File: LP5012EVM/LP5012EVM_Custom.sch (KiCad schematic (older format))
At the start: 10 parts, among them J1 Main Connector, U1 LP5012

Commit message: Corrección de errores y actualizacion de nombres
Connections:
- net VBG is gone; now on net VCC: D1.4 (BA), D1.5 (GA), D2.4 (BA), D2.5 (GA), D3.4 (BA), D3.5 (GA), D4.4 (BA), D4.5 (GA)
- net VR is gone; now on net VCC: D1.6 (RA), D2.6 (RA), D3.6 (RA), D4.6 (RA)
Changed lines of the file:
@@
 EESchema Schematic File Version 4
-LIBS:LP5012EVM-cache
 EELAYER 30 0
 EELAYER END
@@
 Text Label 9050 5300 2    50   ~ 0
 LB10
-Text Label 9750 2100 0    50   ~ 0
-VR
-Text Label 9750 2300 0    50   ~ 0
-VBG
-Text Label 9750 2500 0    50   ~ 0
-VBG
-Wire Wire Line
-	9600 2100 9750 2100
-Wire Wire Line
-	9600 2300 9750 2300
-Wire Wire Line
-	9600 2500 9750 2500
-Text Label 9750 4150 0    50   ~ 0
-VR
-Text Label 9750 4350 0    50   ~ 0
-VBG
-Text Label 9750 4550 0    50   ~ 0
-VBG
-Wire Wire Line
-	9600 4150 9750 4150
-Wire Wire Line
-	9600 4350 9750 4350
-Wire Wire Line
-	9600 4550 9750 4550
-Text Label 9750 5100 0    50   ~ 0
-VR
-Text Label 9750 5300 0    50   ~ 0
-VBG
-Text Label 9750 5500 0    50   ~ 0
-VBG
-Wire Wire Line
-	9600 5100 9750 5100
-Wire Wire Line
-	9600 5300 9750 5300
-Wire Wire Line
-	9600 5500 9750 5500
-Text Label 9750 3050 0    50   ~ 0
-VR
-Text Label 9750 3250 0    50   ~ 0
-VBG
-Text Label 9750 3450 0    50   ~ 0
-VBG
-Wire Wire Line
-	9600 3050 9750 3050
-Wire Wire Line
-	9600 3250 9750 3250
-Wire Wire Line
-	9600 3450 9750 3450
 Text Label 7600 7500 0    79   ~ 0
 LP5012_Custom_PCB
@@
 Wire Wire Line
 	5450 3650 5450 3900
-Text Notes 6400 3600 0    50   ~ 0
+Text Notes 5650 4050 0    50   ~ 0
 Via Layout Design from the chip manufacturer.\nPage 45: http://www.ti.com/lit/ds/symlink/lp5012.pdf\n
 Wire Wire Line
@@
 Text Notes 4150 3650 0    50   ~ 0
 Iset(3.3k) = 22.3mA
+$Comp
+L power:VCC #PWR0107
+U 1 1 5D98000B
+P 9900 1950
+F 0 "#PWR0107" H 9900 1800 50  0001 C CNN
+F 1 "VCC" H 9917 2123 50  0000 C CNN
+F 2 "" H 9900 1950 50  0001 C CNN
+F 3 "" H 9900 1950 50  0001 C CNN
+	1    9900 1950
+	1    0    0    -1
+$EndComp
+$Comp
+L power:VCC #PWR0110
+U 1 1 5D981315
+P 9900 2900
+F 0 "#PWR0110" H 9900 2750 50  0001 C CNN
+F 1 "VCC" H 9917 3073 50  0000 C CNN
+F 2 "" H 9900 2900 50  0001 C CNN
+F 3 "" H 9900 2900 50  0001 C CNN
+	1    9900 2900
+	1    0    0    -1
+$EndComp
+$Comp
+L power:VCC #PWR0111
+U 1 1 5D981A4D
+P 9900 4000
+F 0 "#PWR0111" H 9900 3850 50  0001 C CNN
+F 1 "VCC" H 9917 4173 50  0000 C CNN
+F 2 "" H 9900 4000 50  0001 C CNN
+F 3 "" H 9900 4000 50  0001 C CNN
+	1    9900 4000
+	1    0    0    -1
+$EndComp
+$Comp
+L power:VCC #PWR0112
+U 1 1 5D981FA3
+P 9950 4950
+F 0 "#PWR0112" H 9950 4800 50  0001 C CNN
+F 1 "VCC" H 9967 5123 50  0000 C CNN
+F 2 "" H 9950 4950 50  0001 C CNN
+F 3 "" H 9950 4950 50  0001 C CNN
+	1    9950 4950
+	1    0    0    -1
+$EndComp
+Wire Wire Line
+	9900 2500 9900 2300
+Wire Wire Line
+	9600 2500 9900 2500
+Connection ~ 9900 2100
+Wire Wire Line
+	9900 2100 9900 1950
+Wire Wire Line
+	9600 2100 9900 2100
+Connection ~ 9900 2300
+Wire Wire Line
+	9900 2300 9900 2100
+Wire Wire Line
+	9900 3450 9900 3250
+Wire Wire Line
+	9600 3450 9900 3450
+Wire Wire Line
+	9600 3050 9900 3050
+Connection ~ 9900 3050
+Wire Wire Line
+	9900 3050 9900 2900
+Wire Wire Line
+	9600 3250 9900 3250
+Connection ~ 9900 3250
+Wire Wire Line
+	9900 3250 9900 3050
+Wire Wire Line
+	9900 4550 9900 4350
+Wire Wire Line
+	9600 4550 9900 4550
+Wire Wire Line
+	9600 4150 9900 4150
+Connection ~ 9900 4150
+Wire Wire Line
+	9900 4150 9900 4000
+Wire Wire Line
+	9600 4350 9900 4350
+Connection ~ 9900 4350
+Wire Wire Line
+	9900 4350 9900 4150
+Wire Wire Line
+	9950 5500 9950 5300
+Wire Wire Line
+	9600 5500 9950 5500
+Wire Wire Line
+	9600 5100 9950 5100
+Connection ~ 9950 5100
+Wire Wire Line
+	9950 5100 9950 4950
+Wire Wire Line
+	9600 5300 9950 5300
+Connection ~ 9950 5300
+Wire Wire Line
+	9950 5300 9950 5100
+Wire Wire Line
+	9600 2300 9900 2300
 $EndSCHEMATC

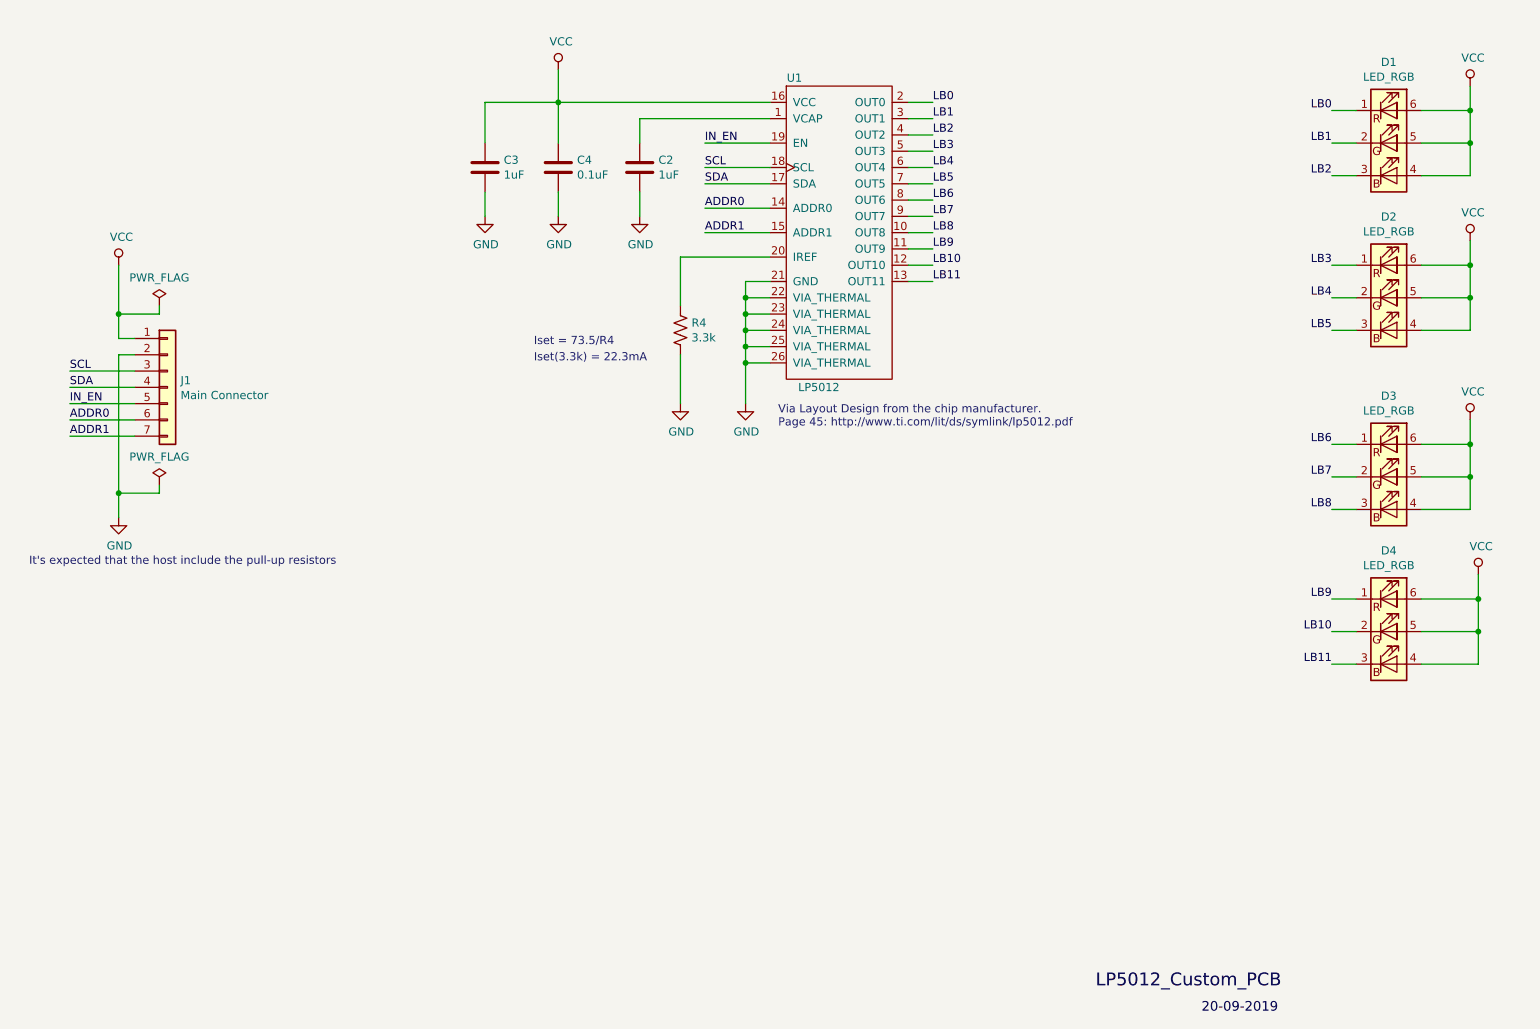
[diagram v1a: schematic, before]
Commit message: Corregidos algunos aspectos del revisor
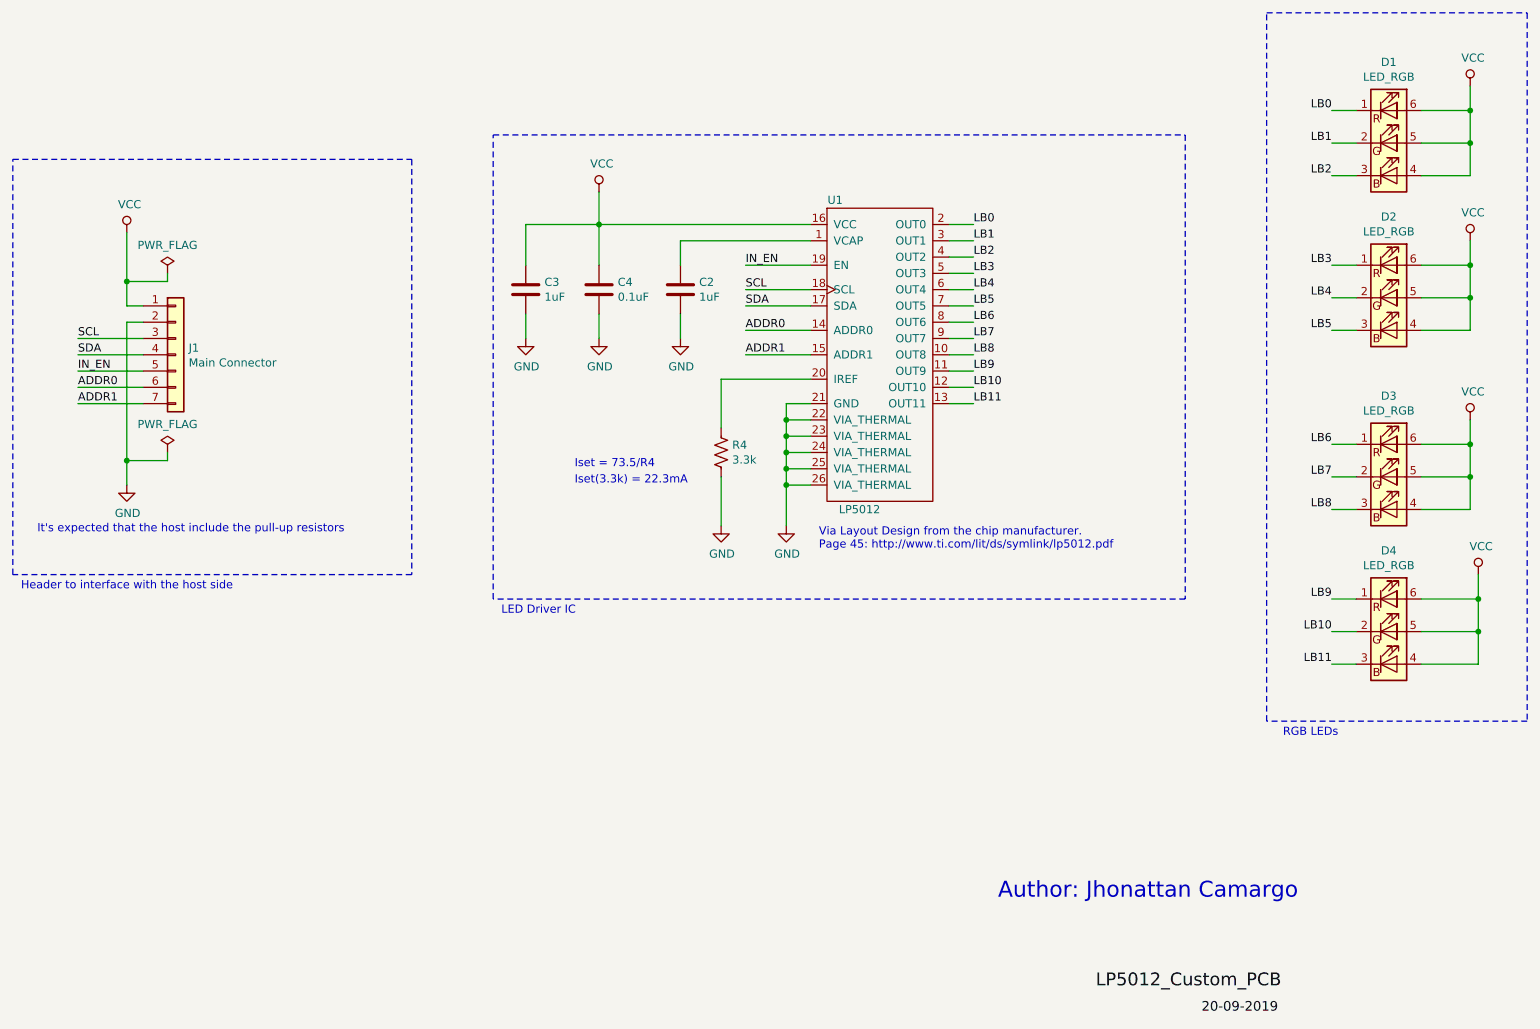
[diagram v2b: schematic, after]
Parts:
- C2, C3, C4: footprint (none) -> Capacitor_SMD:C_0805_2012Metric
- D1, D2, D3, D4: footprint (none) -> LED_SMD:LED_RGB_5050-6
- J1: footprint (none) -> Connector_PinHeader_2.54mm:PinHeader_1x07_P2.54mm_Vertical
- R4: footprint (none) -> Resistor_SMD:R_0805_2012Metric
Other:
- note added: "Author: Jhonattan Camargo"
- note added: "Header to interface with the host side"
- note added: "LED Driver IC"
- note added: "RGB LEDs"
- moved on the sheet: C2, C3, C4, J1, R4, U1
